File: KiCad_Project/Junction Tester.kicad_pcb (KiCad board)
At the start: 2 copper layers, 62 x 39.6 mm, 14 parts, among them J1 Conn_02x06_Counter_Clockwise, J2 Conn_02x06_Counter_Clockwise, J3 Conn_01x02_Male, J4 Conn_01x02_Male, J5 Conn_01x02_Male, U1 3PoleSwitch, U2 3PoleSwitch, U3 NCP1117-1.5_SOT223

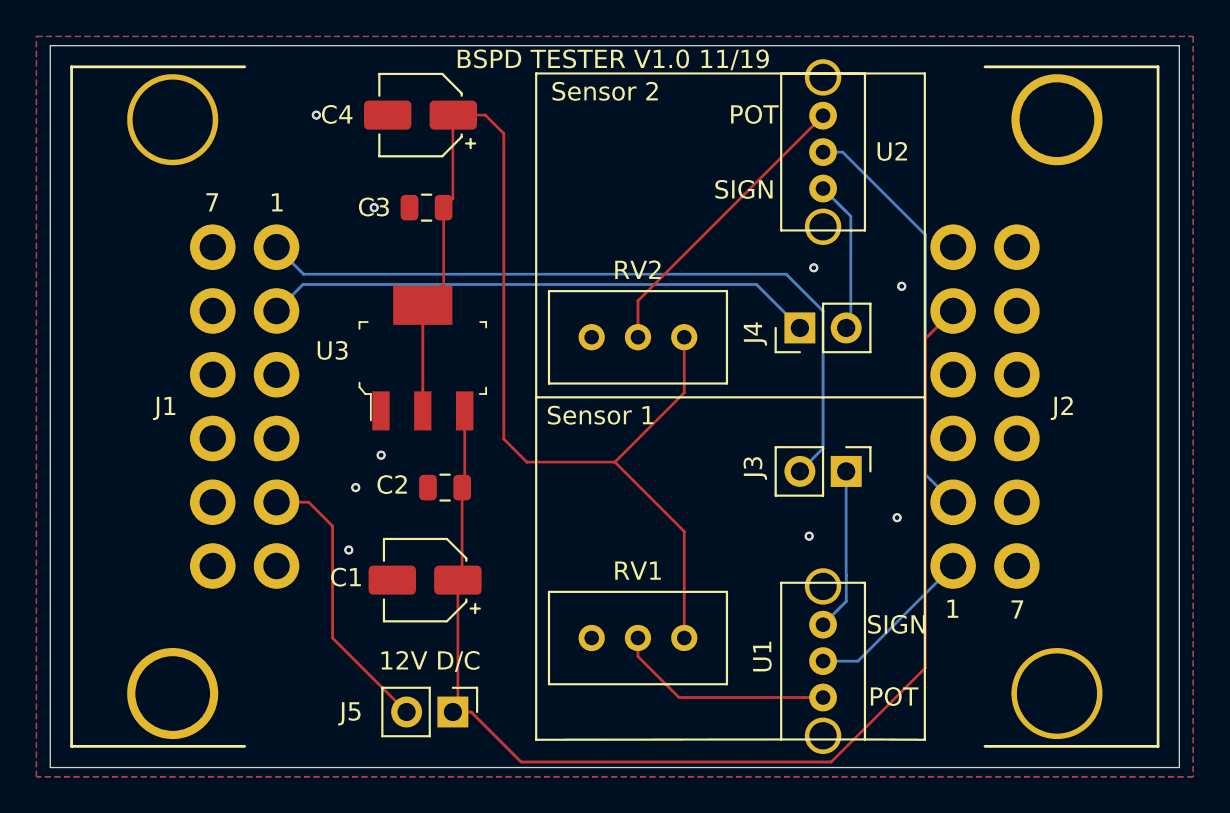
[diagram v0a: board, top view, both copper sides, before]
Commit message: Clarified some silk screen
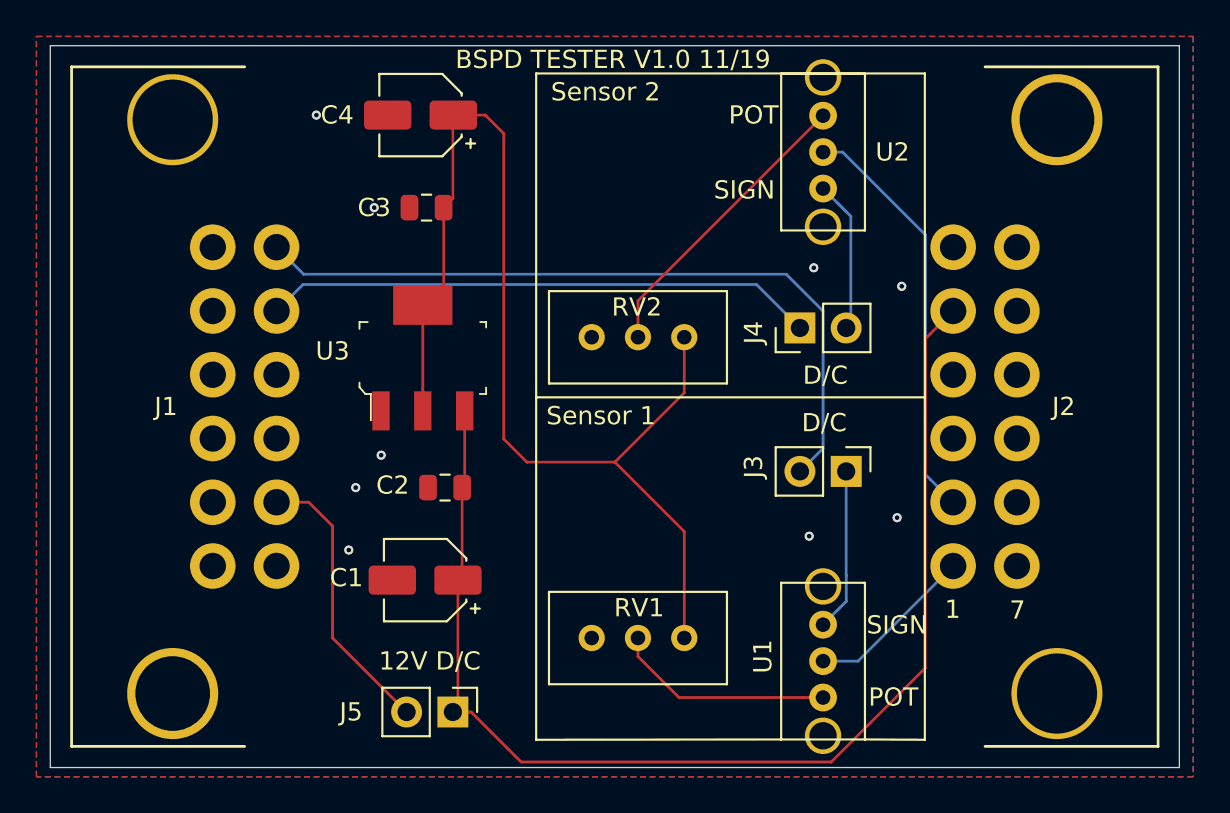
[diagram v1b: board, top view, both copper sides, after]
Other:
- board text added: "D/C"
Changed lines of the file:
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@@
     (descr "Potentiometer, vertical, Bourns 3296W, https://www.bourns.com/pdfs/3296.pdf")
     (tags "Potentiometer vertical Bourns 3296W")
-    (fp_text reference RV2 (at -2.54 -3.66) (layer F.SilkS)
+    (fp_text reference RV2 (at -2.6035 -1.651) (layer F.SilkS)
       (effects (font (size 1 1) (thickness 0.15)))
     )
@@
     (descr "Potentiometer, vertical, Bourns 3296W, https://www.bourns.com/pdfs/3296.pdf")
     (tags "Potentiometer vertical Bourns 3296W")
-    (fp_text reference RV1 (at -2.54 -3.66) (layer F.SilkS)
+    (fp_text reference RV1 (at -2.4765 -1.651) (layer F.SilkS)
       (effects (font (size 1 1) (thickness 0.15)))
     )
@@
     )
   )
+  (gr_text D/C (at 185.547 92.2655) (layer F.SilkS)
+    (effects (font (size 1 1) (thickness 0.15)))
+  )
+  (gr_text D/C (at 185.4835 94.869) (layer F.SilkS)
+    (effects (font (size 1 1) (thickness 0.15)))
+  )
   (gr_text "Sensor 1" (at 173.228 94.488) (layer F.SilkS)
     (effects (font (size 1 1) (thickness 0.15)))
@@
     (effects (font (size 1 1) (thickness 0.15)))
   )
-  (gr_text 1 (at 155.448 82.804) (layer F.SilkS)
-    (effects (font (size 1 1) (thickness 0.15)))
-  )
-  (gr_text "7\n" (at 151.892 82.804) (layer F.SilkS)
-    (effects (font (size 1 1) (thickness 0.15)))
-  )
